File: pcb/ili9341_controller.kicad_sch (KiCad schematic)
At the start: 162 parts, among them J1 USB_B_Micro, J2 RP_SWD_CONN, J3 CONN_RP2040, J4 CONN_FPGA, J5 CONN_TFT, J6 CONN_PWR, J7 PWR_JUMPERS, Q1 NPN, Q2 NPN, Q3 NPN, SW1 RP_RST_SW, SW10 SW_BUTTON_B, SW2 RP_USB_BOOT_SW, SW3 SW_ARROW_UP, SW4 SW_ARROW_DOWN, SW5 SW_ARROW_LEFT, SW6 SW_ARROW_RIGHT, SW7 SW_BUTTON_START, SW8 SW_BUTTON_SEL, SW9 SW_BUTTON_A, U1 ICE40UP5K-SG48ITR, U2 LM3880, U3 TLV75512PDBV, U4 TLV75525PDBV, U5 TLV75533PDBV, U6 RP2040, U7 W25Q128JVS, U9 74LS151, Y1 12MHz

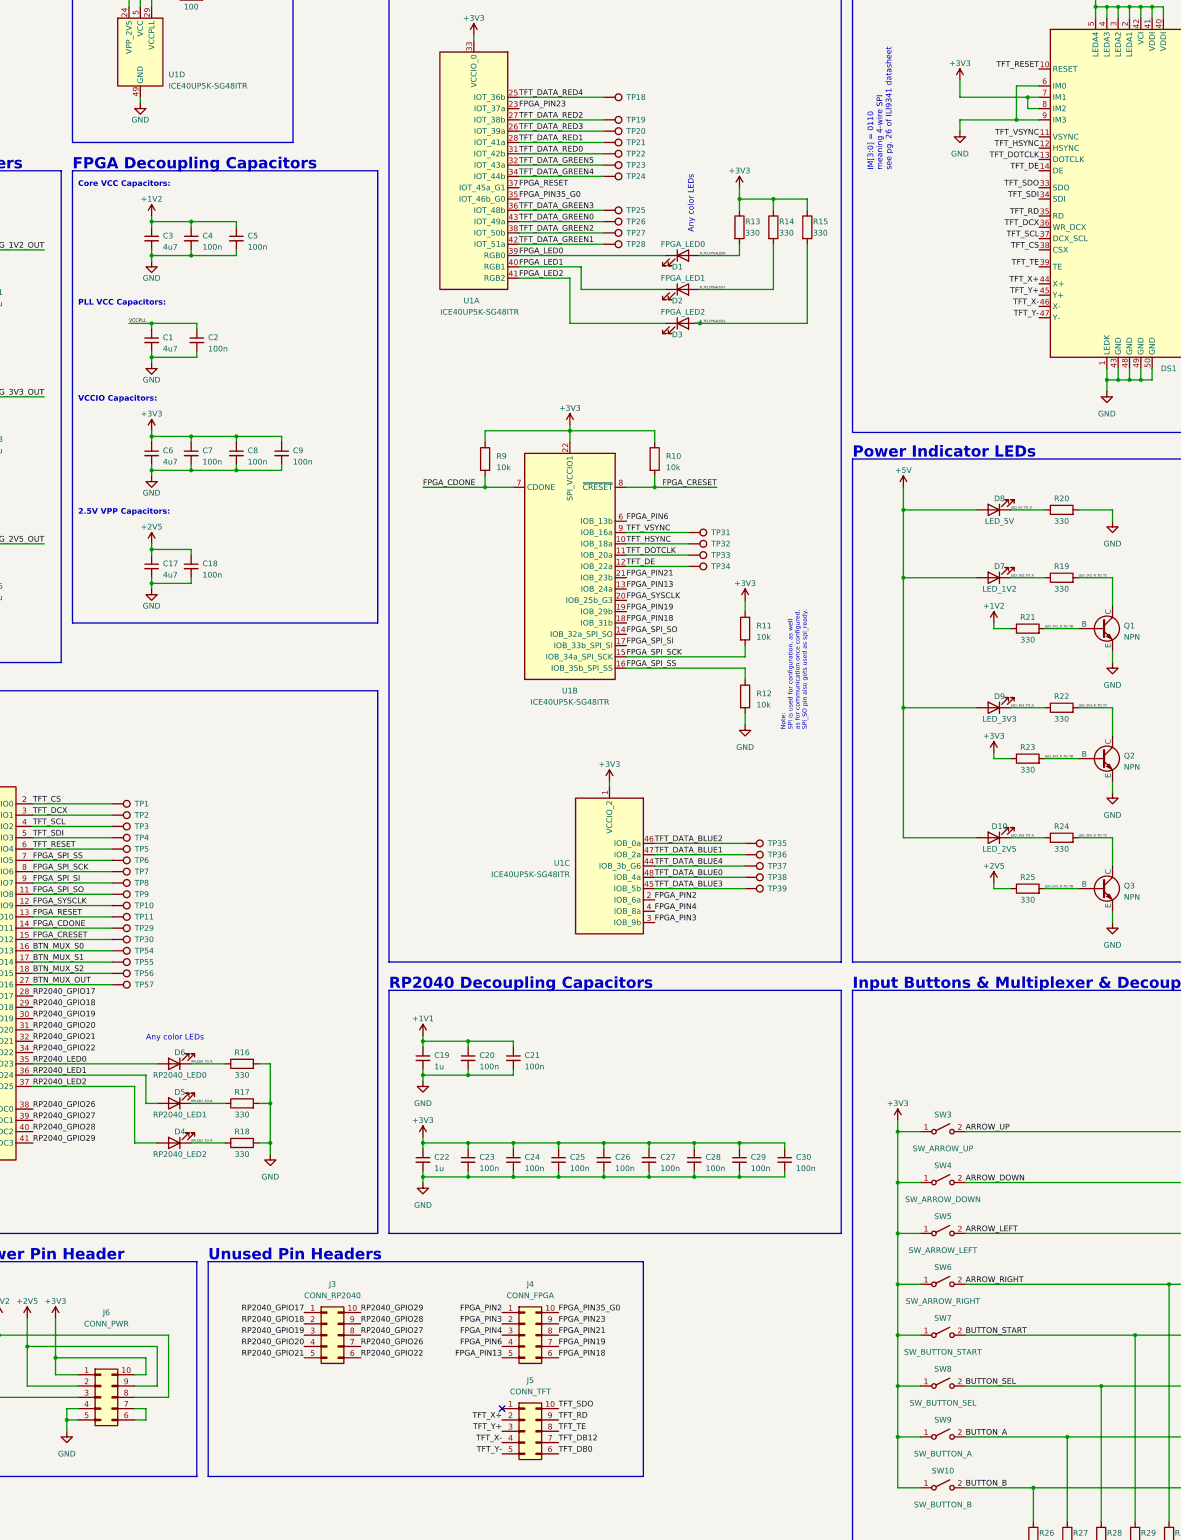
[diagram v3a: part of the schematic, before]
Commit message: assign (tentative) footprints to every component
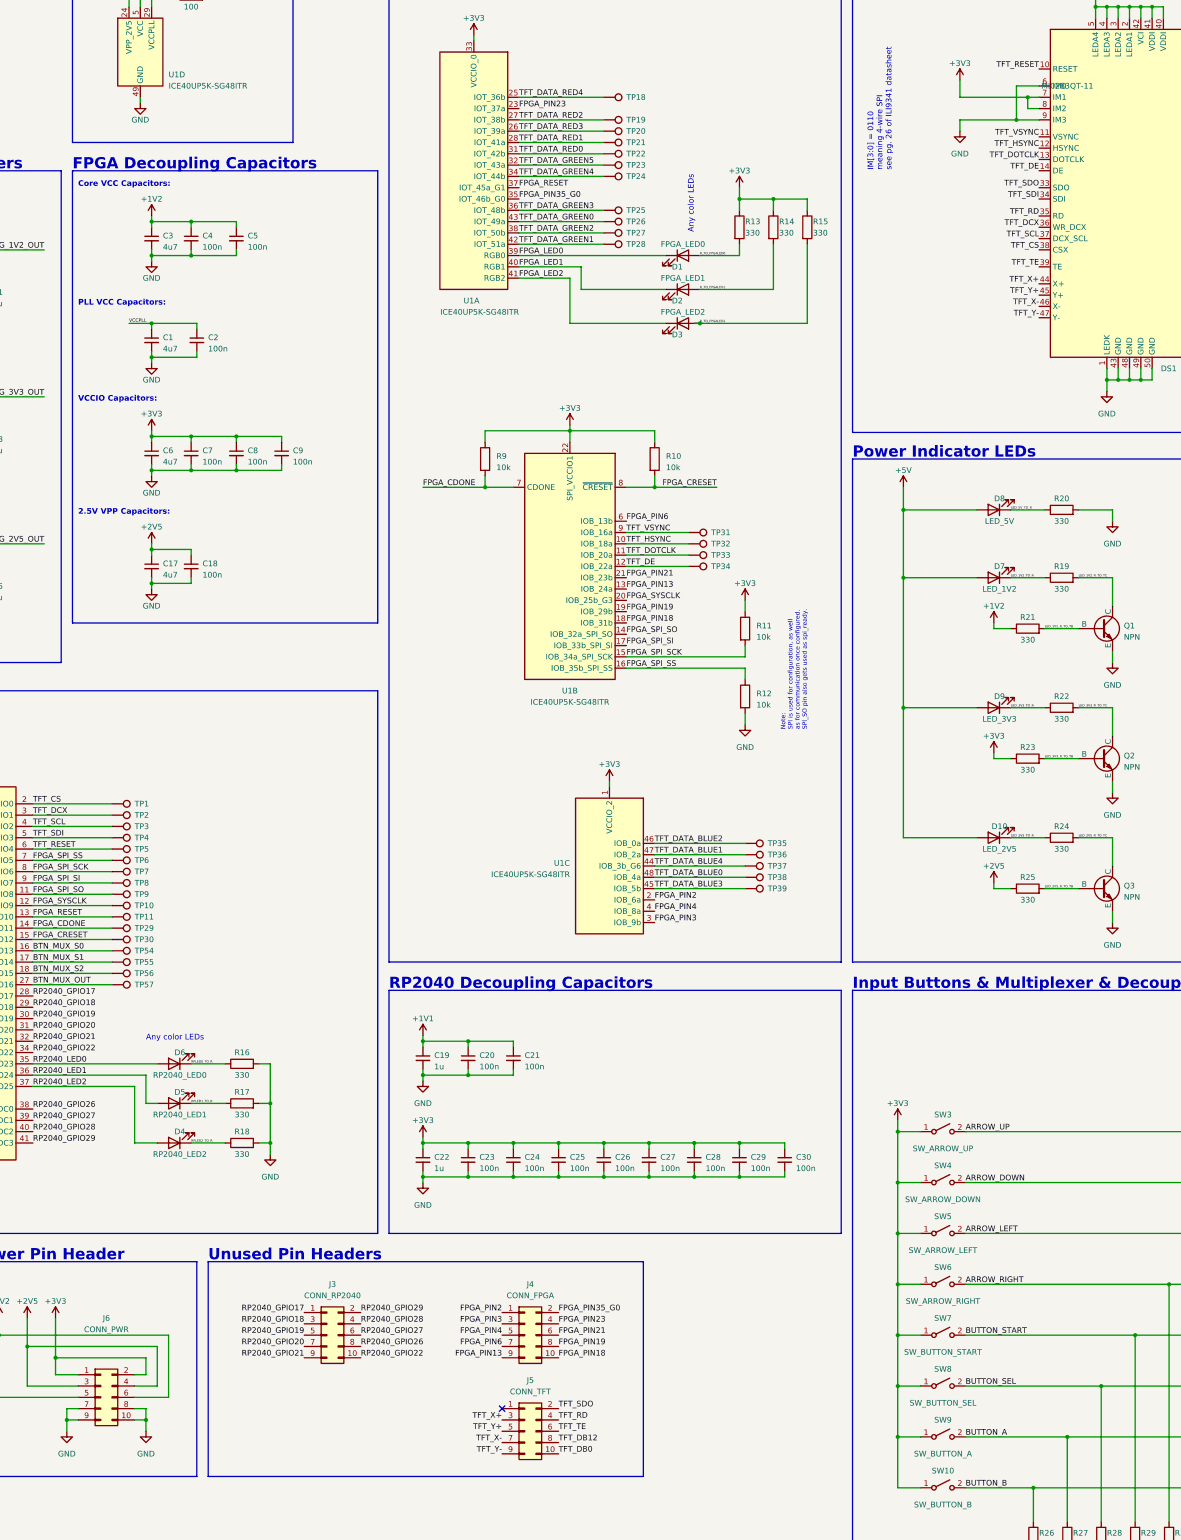
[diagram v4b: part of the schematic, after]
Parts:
- removed J6: CONN_PWR, symbol Connector_Generic:Conn_02x05_Counter_Clockwise
- added J6: CONN_PWR, Connector_PinHeader_2.54mm:PinHeader_2x05_P2.54mm_Vertical, symbol Connector_Generic:Conn_02x05_Odd_Even
- C1, C10, C11, C12, C13, C14, C15, C16, C17, C18, C19, C2, C20, C21, C22, C23, C24, C25, C26, C27, C28, C29, C3, C30, C31, C32, C33, C34, C35, C4, C5, C6, C7, C8, C9: footprint (none) -> Capacitor_SMD:C_0603_1608Metric_Pad1.08x0.95mm_HandSolder
- D1, D10, D2, D3, D4, D5, D6, D7, D8, D9: footprint (none) -> LED_SMD:LED_0603_1608Metric_Pad1.05x0.95mm_HandSolder
- DS1: value ~ -> MI0283QT-11; footprint (none) -> Connector_FFC-FPC:TE_5-1734839-0_1x50-1MP_P0.5mm_Horizontal
- J1: footprint (none) -> Connector_USB:USB_Micro-B_Molex-105017-0001
- J2: footprint (none) -> Connector_PinHeader_2.54mm:PinHeader_1x03_P2.54mm_Vertical
- J3, J4, J5: footprint (none) -> Connector_PinHeader_2.54mm:PinHeader_2x05_P2.54mm_Vertical; symbol Connector_Generic:Conn_02x05_Counter_Clockwise -> Connector_Generic:Conn_02x05_Odd_Even
- J7: footprint (none) -> Connector_PinHeader_2.54mm:PinHeader_2x05_P2.54mm_Vertical
- Q1, Q2, Q3: footprint (none) -> Package_TO_SOT_SMD:SOT-23-3
- R1, R10, R11, R12, R13, R14, R15, R16, R17, R18, R19, R2, R20, R21, R22, R23, R24, R25, R26, R27, R28, R29, R3, R30, R31, R32, R33, R4, R5, R6, R7, R8, R9: footprint (none) -> Resistor_SMD:R_0603_1608Metric_Pad0.98x0.95mm_HandSolder
- SW1, SW10, SW2, SW3, SW4, SW5, SW6, SW7, SW8, SW9: footprint (none) -> Button_Switch_SMD:SW_SPST_PTS645
- TP1, TP10, TP11, TP15, TP16, TP17, TP18, TP19, TP2, TP20, TP21, TP22, TP23, TP24, TP25, TP26, TP27, TP28, TP29, TP3, TP30, TP31, TP32, TP33, TP34, TP35, TP36, TP37, TP38, TP39, TP4, TP40, TP41, TP42, TP43, TP44, TP45, TP46, TP47, TP48, TP49, TP5, TP50, TP51, TP52, TP53, TP54, TP55, TP56, TP57, TP6, TP7, TP8, TP9: footprint (none) -> TestPoint:TestPoint_Pad_1.0x1.0mm
- U9: footprint (none) -> Package_SO:SOIC-16_3.9x9.9mm_P1.27mm
- Y1: footprint (none) -> Local:XTAL_ABLS2-12.000MHZ-D4Y-T
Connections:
- net +1V2: now also J6.5 (Pin_5), J6.6 (Pin_6)
- net +2V5: now also J6.3 (Pin_3), J6.4 (Pin_4)
- net +3V3: now also J6.1 (Pin_1), J6.2 (Pin_2)
- net FPGA_PIN13: now also J4.9 (Pin_9); no longer J4.5 (Pin_5)
- net FPGA_PIN18: now also J4.10 (Pin_10); no longer J4.6 (Pin_6)
- net FPGA_PIN19: now also J4.8 (Pin_8); no longer J4.7 (Pin_7)
- net FPGA_PIN21: now also J4.6 (Pin_6); no longer J4.8 (Pin_8)
- net FPGA_PIN23: now also J4.4 (Pin_4); no longer J4.9 (Pin_9)
- net FPGA_PIN3: now also J4.3 (Pin_3); no longer J4.2 (Pin_2)
- net FPGA_PIN35_G0: now also J4.2 (Pin_2); no longer J4.10 (Pin_10)
- net FPGA_PIN4: now also J4.5 (Pin_5); no longer J4.3 (Pin_3)
- net FPGA_PIN6: now also J4.7 (Pin_7); no longer J4.4 (Pin_4)
- net GND: now also J6.10 (Pin_10), J6.7 (Pin_7), J6.8 (Pin_8), J6.9 (Pin_9)
- net RP2040_GPIO18: now also J3.3 (Pin_3); no longer J3.2 (Pin_2)
- net RP2040_GPIO19: now also J3.5 (Pin_5); no longer J3.3 (Pin_3)
- net RP2040_GPIO20: now also J3.7 (Pin_7); no longer J3.4 (Pin_4)
- net RP2040_GPIO21: now also J3.9 (Pin_9); no longer J3.5 (Pin_5)
- net RP2040_GPIO22: now also J3.10 (Pin_10); no longer J3.6 (Pin_6)
- net RP2040_GPIO26: now also J3.8 (Pin_8); no longer J3.7 (Pin_7)
- net RP2040_GPIO27: now also J3.6 (Pin_6); no longer J3.8 (Pin_8)
- net RP2040_GPIO28: now also J3.4 (Pin_4); no longer J3.9 (Pin_9)
- net RP2040_GPIO29: now also J3.2 (Pin_2); no longer J3.10 (Pin_10)
- net TFT_DB0: now also J5.10 (Pin_10); no longer J5.6 (Pin_6)
- net TFT_DB12: now also J5.8 (Pin_8); no longer J5.7 (Pin_7)
- net TFT_RD: now also J5.4 (Pin_4); no longer J5.9 (Pin_9)
- net TFT_SDO: now also J5.2 (Pin_2); no longer J5.10 (Pin_10)
- net TFT_TE: now also J5.6 (Pin_6); no longer J5.8 (Pin_8)
- net TFT_X+: now also J5.3 (Pin_3); no longer J5.2 (Pin_2)
- net TFT_X-: now also J5.7 (Pin_7); no longer J5.4 (Pin_4)
- net TFT_Y+: now also J5.5 (Pin_5); no longer J5.3 (Pin_3)
- net TFT_Y-: now also J5.9 (Pin_9); no longer J5.5 (Pin_5)

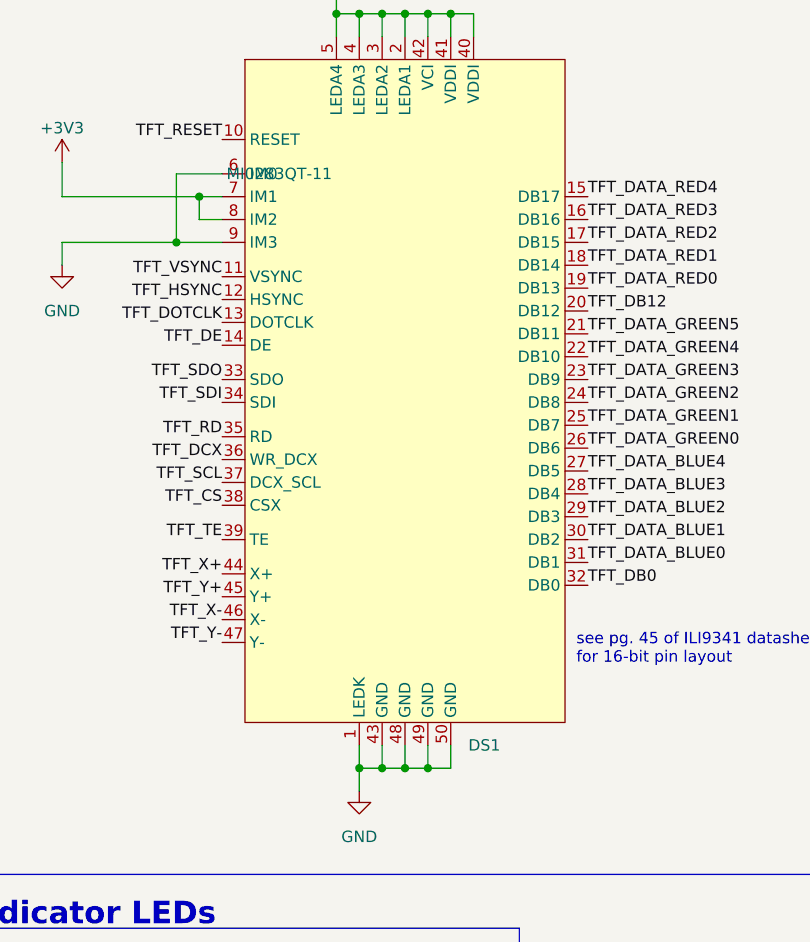
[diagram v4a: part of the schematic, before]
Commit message: create pcb file, add 3d models to all components
the 50 pin FPC connector 3d model was swapped with a 25-pin one (due to a lack of a 50 pin one), but the sizes of the models are the same and that's all that really matters
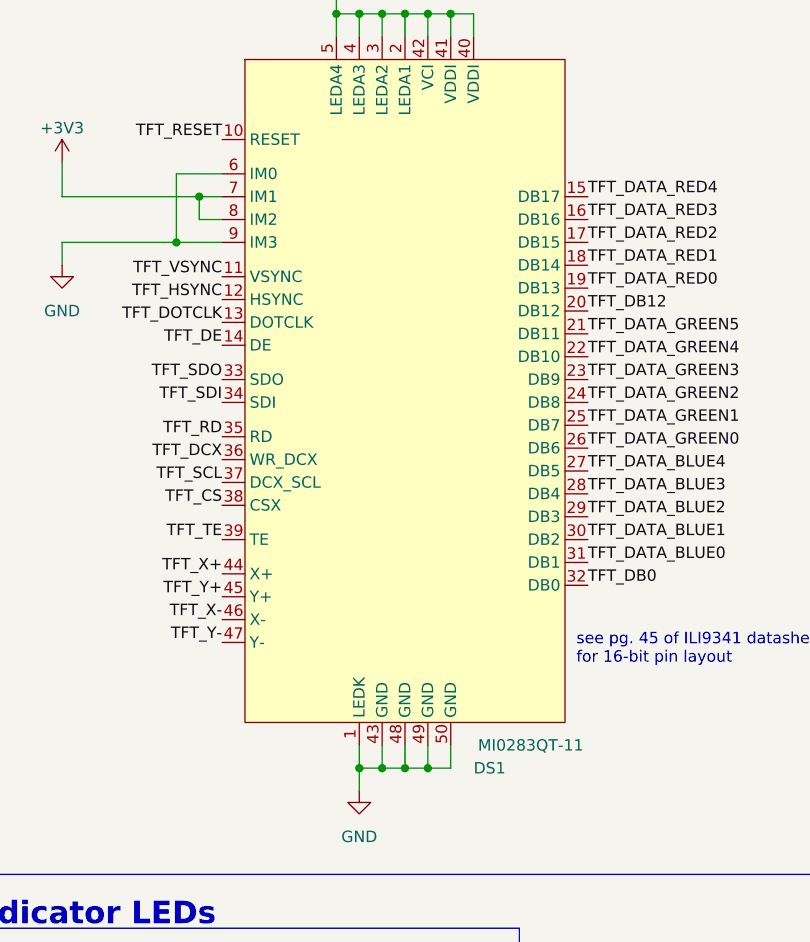
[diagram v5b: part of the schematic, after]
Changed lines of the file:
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@@
   )
   (symbol (lib_id "MI0283QT-11:MI0283QT-11") (at 367.03 48.26 0) (unit 1)
-    (in_bom yes) (on_board yes) (dnp no) (fields_autoplaced)
-    (property "Reference" "DS1" (at 391.8459 124.46 0)
+    (in_bom yes) (on_board yes) (dnp no)
+    (property "Reference" "DS1" (at 392.43 127 0)
       (effects (font (size 1.27 1.27)) (justify left))
     )
-    (property "Value" "MI0283QT-11" (at 370.84 60.96 0)
+    (property "Value" "MI0283QT-11" (at 398.78 124.46 0)
       (effects (font (size 1.27 1.27)))
     )

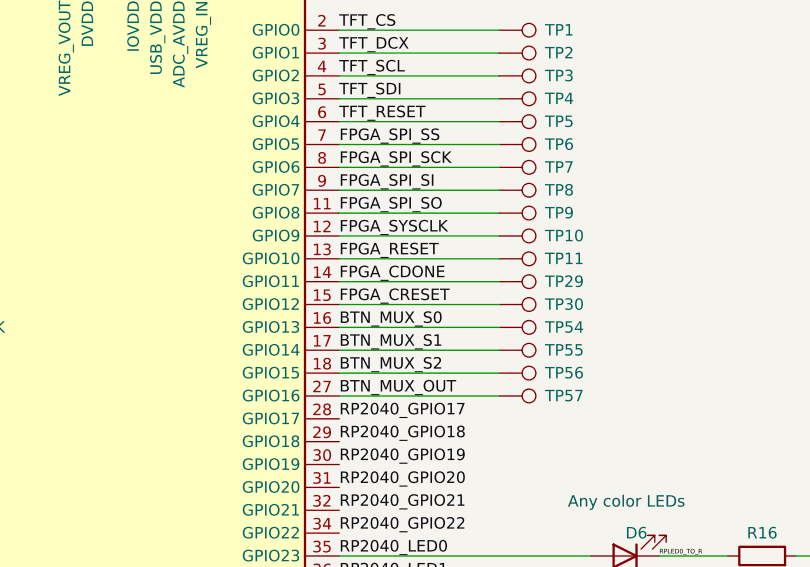
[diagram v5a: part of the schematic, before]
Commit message: place and route out all components
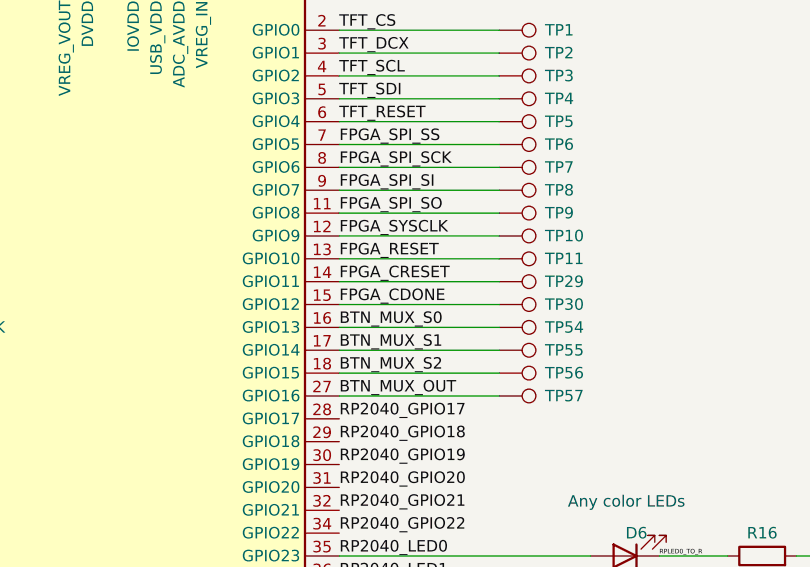
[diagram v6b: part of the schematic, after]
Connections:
- net FPGA_CDONE: now also TP30.1, U6.15 (GPIO12); no longer TP29.1, U6.14 (GPIO11)
- net FPGA_CRESET: now also TP29.1, U6.14 (GPIO11); no longer TP30.1, U6.15 (GPIO12)
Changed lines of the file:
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@@
+    (effects (font (size 1.27 1.27)) (justify left bottom))
+  )
+  (label "FPGA_CRESET" (at 138.43 250.19 0) (fields_autoplaced)
     (effects (font (size 1.27 1.27)) (justify left bottom))
   )
@@
     (effects (font (size 1.27 1.27)) (justify right bottom))
   )
+  (label "FPGA_CDONE" (at 138.43 252.73 0) (fields_autoplaced)
+    (effects (font (size 1.27 1.27)) (justify left bottom))
+  )
   (label "TFT_DATA_GREEN0" (at 405.13 91.44 0) (fields_autoplaced)
     (effects (font (size 1.27 1.27)) (justify left bottom))
@@
   (label "BTN_MUX_S0" (at 477.52 318.77 180) (fields_autoplaced)
     (effects (font (size 1.27 1.27)) (justify right bottom))
-  )
-  (label "FPGA_CRESET" (at 138.43 252.73 0) (fields_autoplaced)
-    (effects (font (size 1.27 1.27)) (justify left bottom))
   )
   (label "LED_3V3_R_TO_TB" (at 365.76 212.09 0) (fields_autoplaced)
@@
     (effects (font (size 1.27 1.27)) (justify right bottom))
   )
-  (label "FPGA_CDONE" (at 138.43 250.19 0) (fields_autoplaced)
-    (effects (font (size 1.27 1.27)) (justify left bottom))
-  )
   (label "TFT_DATA_GREEN2" (at 247.65 93.98 0) (fields_autoplaced)
